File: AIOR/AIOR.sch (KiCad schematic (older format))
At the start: 92 parts, among them J1 Conn_01x06, J2 Conn_01x02, P1 CONN_02X20, P2 CONN_01X02, P3 CONN_01X04, P8 CONN_01X02, P9 CONN_01X04, U1 MCP2517FD, U2 ISO1050, U3 P82B715, U4 SI8641-SOIC, Y1 4MHz

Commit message: AIOR start
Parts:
- added D? (x2): BAT43, Diode_SMD:D_SOD-323_HandSoldering, symbol Diode:BAT43
- added R? (x3): 3k3, Resistors_SMD:R_0805_HandSolderingII, symbol AIOR-rescue:R
- added U?: DSPIC33EP128GM604, QFN/TQFP44, symbol dsPIC33EP128GM604:DSPIC33EP128GM604
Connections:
- net +3V3: now also U?.16 (BVDD)
- net GND: now also U?.9 (BGND)
- net GNDA: now also U?.16 (AVSS), U?.29 (VSS), U?.39 (VSS), U?.6 (VSS)
- net RxD: now also U?.13 (BOUT)
- net TxD: now also U?.12 (BDIN)
- net RS485_EN: now reaches U?.2 (~RE~), U?.3 (DE)
- net at U?.5 (AOUT): now also R?.2, U?.23 (PGEC1/OA1IN+/AN4/RPI34/RB2)
- net at U?.6 (ASCL): now also R?.2, U?.24 (PGED1/OA1IN-/AN5/CTMUC/RP35/RB3)
- new net: R?.1, U?.18 (~MCLR)
- new net: D?.1 (K), D?.2 (A), R?.2
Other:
- moved on the sheet: C6, C7, C8, C?, D?, J1, J2, J?, P8, P9, P?, Q?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

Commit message: wip
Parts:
- added C? (x4): 100nF, Capacitors_SMD:C_0805_HandSoldering, symbol AIOR-rescue:C
- added C? (x7): 1nF, Capacitors_SMD:C_0805_HandSoldering, symbol AIOR-rescue:C
- added C?: 560pF, Capacitors_SMD:C_0805_HandSoldering, symbol AIOR-rescue:C
- added D? (x2): 1N4148W, Diode_SMD:D_SOD-123, symbol Diode:1N4148W
- added Q? (x2): BC857, Package_TO_SOT_SMD:SOT-23, symbol Transistor_BJT:BC857
- added R?: 1M, Resistors_SMD:R_0805_HandSolderingII, symbol AIOR-rescue:R
- added R?: 2k2, Resistors_SMD:R_0805_HandSolderingII, symbol AIOR-rescue:R
- added R? (x3): 0, Resistors_SMD:R_0805_HandSolderingII, symbol AIOR-rescue:R
- added R? (x2): 3k3, Resistors_SMD:R_0805_HandSolderingII, symbol AIOR-rescue:R
- added R? (x2): 8k2, Resistors_SMD:R_0805_HandSolderingII, symbol AIOR-rescue:R
- added R?: 18k, Resistors_SMD:R_0805_HandSolderingII, symbol AIOR-rescue:R
- added R? (x2): 4k7, Resistors_SMD:R_0805_HandSolderingII, symbol AIOR-rescue:R
- added R?: 1k, Resistors_SMD:R_0805_HandSolderingII, symbol AIOR-rescue:R
- added U?: L7833, Package_TO_SOT_SMD:TO-252-3_TabPin2, symbol Regulator_Linear:L7805
- R?: value 10k -> 4k7
- renumbered C3 to C2, C1 to C3, R2 to R1, R1 to R2
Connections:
- net +5VA: now also C?.1, Q?.2 (E), R?.2
- net B_SENSE: now also R?.1, R?.2, U?.13 (P2.5/AD13), D?.1 (K), D?.2 (A), R?.1, R?.1, R?.1; no longer U?.6 (IS)
- net GNDA: now also U?.10 (TEST), U?.11 (VSSD), U?.6 (VSSA), U?.9 (MODE), C?.1, C?.2, C?.2, C?.2, C?.2, C?.2, C?.2, C?.2, C?.2, D?.1 (K), D?.2 (A), R?.1, R?.1, R?.1, U?.2 (GND)
- net VCC: now also C?.1, R?.2, U?.1 (IN)
- net Vccm: now reaches U?.11 (P2.7/AD15)
- net Vccm: now also C?.1, R?.1, R?.2
- net at U?.12 (P2.6/AD14): now also C?.1, R?.2
- net SUBC: now reaches U?.14 (P2.4/AD12)
- net SUBC: now also C?.1, Q?.3 (C), R?.2
- net RDDA: now reaches U?.19 (P1.7/AD7)
- net RDDA: now also U?.2 (RDDA)
- net RDCL: now reaches U?.20 (P1.6/AD6)
- net RDCL: now also U?.16 (RDCL)
- net QUAL: now reaches U?.21 (P1.5/AD5)
- net QUAL: now also U?.1 (QUAL)
- net at U?.29 (P0.5/UART0-RX): now also R?.1
- net at U?.30 (P0.4/UART0-TX): now also R?.1
- net IS_LEFT: now reaches R?.1, U?.6 (IS)
- net IS_LEFT: no longer R?.1, R?.2
- net at C?.1, U?.13 (OSCI), Y?.2: now also R?.2
- net at C?.1, Y?.1: now also R?.1, R?.1; no longer U?.14 (OSCO)
- net T57: now reaches U?.15 (T57)
- net at U?.3 (Vref): now also U?.4 (MUX), C?.1, C?.1
- net at U?.5 (VDDA): now also C?.1, R?.1
- net at U?.7 (CIN): now also C?.1
- net at U?.8 (SCOUT): now also C?.1, C?.2
- new net: R?.2, U?.14 (OSCO)
- new net: C?.2, R?.1
- new net: Q?.1 (B), Q?.2 (E), R?.2
- new net: Q?.1 (B), Q?.3 (C), R?.2
- new net: C?.2, C?.2, R?.2
- new net: C?.1, U?.3 (OUT)
- new net IS_RIGHT: R?.2, U?.6 (IS)
- no-connect marks 30 -> 32
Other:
- moved on the sheet: C?, R?, U?, Y?

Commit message: wip
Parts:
- removed D?: BAT43, Diode_SMD:D_SOD-323_HandSoldering, symbol Diode:BAT43
- removed J2: Conn_01x02, Pin_Headers:Pin_Header_Straight_1x02_Pitch2.54mm, symbol AIOR-rescue:Conn_01x02
- removed R8: 0, Resistors_SMD:R_0805_HandSolderingII, symbol AIOR-rescue:R
- removed R9: 50, Resistors_SMD:R_0805_HandSolderingII, symbol AIOR-rescue:R
- added C?: 10uF, Capacitor_SMD:C_Elec_5x5.8, symbol Device:CP
- added C? (x2): 100nF, Capacitors_SMD:C_0805_HandSoldering, symbol AIOR-rescue:C
- added D?: LED, LED_SMD:LED_0805_2012Metric_Pad1.15x1.40mm_HandSolder, symbol Device:LED
- added J?: 5V 12V, symbol Connector_Generic:Conn_01x03
- added P?: Selectrix, w_conn_jst-ph:s4b-ph-kl, symbol AIOR-rescue:CONN_01X04
- added Q?: BC817, Package_TO_SOT_SMD:SOT-23, symbol Transistor_BJT:BC817
- added R? (x2): 1k, Resistors_SMD:R_0805_HandSolderingII, symbol AIOR-rescue:R
- added R?: 470, Resistors_SMD:R_0805_HandSolderingII, symbol AIOR-rescue:R
- added R?: 0, Resistors_SMD:R_0805_HandSolderingII, symbol AIOR-rescue:R
- added R? (x2): 27k, Resistors_SMD:R_0805_HandSolderingII, symbol AIOR-rescue:R
- added R?: 120, Resistors_SMD:R_1206_HandSolderingII, symbol AIOR-rescue:R
- added R?: 1k5, Resistors_SMD:R_0805_HandSolderingII, symbol AIOR-rescue:R
- added U?: MCP2562, Package_SO:SOIC-8_3.9x4.9mm_P1.27mm, symbol AIOR-rescue:MCP2562
- added U?: 4504, Package_SO:SOIC-16_3.9x9.9mm_P1.27mm, symbol 4xxx:4504
- P?: value CONN_01X04 -> Xpressnet
- P?: value CONN_01X04 -> LOCONET
- R? (x2): value 470 -> 1k
- U?: value L7833 -> L7805
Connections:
- net +3V3: now also D?.2 (A), R?.1, R?.1, U?.1 (AVDD), U?.17 (AVDD), U?.28 (VDD), U?.40 (VDD), C?.1, C?.1, D?.2 (A), U?.5 (VIO~)
- net +5VA: now also U?.3 (VDD~)
- net B_ENA: now also U?.11 (RPI45/PWM2L/CTPLS/RB13)
- net B_LEFT: now also U?.14 (RPI46/PWM1H/T3CK/T7CK/RB14)
- net B_RIGHT: now also U?.15 (RPI47/PWM1L/T5CK/T6CK/RB15)
- net B_SENSE: now also U?.19 (OA2OUT/AN0/RPI16/RA0), R?.1; no longer R?.1, R?.2, R?.2
- net CANH: now also P3.4 (P4), R7.2, U2.7 (CANH), U?.7 (CANH); no longer P2.2 (P2), P3.3 (P3), U2.6 (CANL)
- net CANL: now also P2.2 (P2), P3.3 (P3), U2.6 (CANL), U?.6 (CANL); no longer P3.4 (P4), R7.2, U2.7 (CANH)
- net GND: no longer C6.2, C?.2, C?.2, Q?.2 (E), R?.1, R?.1, U4.2 (GND1), U4.8 (GND1), U?.4 (V-)
- net GNDA: now also C6.2, C?.2, C?.2, P?.1 (P1), Q?.2 (E), R?.1, R?.1, U4.2 (GND1), U4.8 (GND1), U?.4 (V-), U?.8 (AGND), C?.2, C?.2, C?.2, P?.1 (P1), Q?.2 (E), U?.2 (VSS~); no longer C7.2, C?.2, C?.2, J1.5 (Pin_5), U4.15 (GND2), U4.9 (GND2), U?.2 (GND)
- net GPIO17: now also U?.13 (BOUT)
- net GPIO4: now also U?.14 (BSDA)
- net LCNET: now also P?.3 (P3), P?.4 (P4)
- net LN_RX: now also U?.4 (RP56/PWM5H/RC8), R?.1; no longer R?.1, R?.2, R?.2, U?.1
- net LN_TX: now also U?.5 (RP57/PWM5L/RC9)
- net QUAL: now also U?.25 (OA3OUT/AN6/RP48/OCFB/RC0)
- net RDCL: now also U?.26 (OA3IN-/AN7/C3IN1-/C4IN1-/RP49/RC1)
- net RDDA: now also U?.27 (AN8/RPI50/U1RTS/BCLK1/FLT3/RC2)
- net RS485_EN: now also U?.10 (RPI44/PWM2H/RB12)
- net RS485_RX: now also U?.8 (RP42/PWM3H/RB10)
- net RS485_TX: now also U?.9 (RP43/PWM3L/RB11)
- net RxD: now also U?.11 (BSCL); no longer U?.13 (BOUT)
- net S88_CLK: now also U?.34 (OA5IN+/AN24/SDO1/RP20/T1CK/RA4)
- net S88_DATA: now also U?.32 (SDA2/RPI24/RA8)
- net S88_LOAD: now also U?.31 (OSC2/CLKO/RPI19/RA3)
- net S88_RST: now also U?.30 (AN32/OSC1/CLKI/RPI18/RA2)
- net VCC: now also C7.1, C?.1, U4.16 (VDD2), U?.3 (OUT), J?.1 (Pin_1), U?.1 (VCC), U?.13 (Select); no longer C?.1, U?.1 (IN)
- net VDDA: now also C?.1, U?.1 (IN), J?.3 (Pin_3); no longer C7.1, U4.16 (VDD2)
- net Vccm: now also U?.20 (OA2IN+/AN1/C2IN1+/RPI17/RA1)
- net at U4.11: now also R?.2
- net at U4.12: now also U?.7 (Cin)
- net at U4.13: now also U?.5 (Bin); no longer J1.3 (Pin_3)
- net at U4.14: now also U?.3 (Ain); no longer J1.2 (Pin_2)
- net at J1.6 (Pin_6): now also R?.1
- net at J1.4 (Pin_4): now also U?.6 (Cout)
- net PLED: now reaches U?.1 (TMS/OA5IN-/AN27/C5IN1-/RP41/RB9)
- net PLED: now also R?.2
- net at U?.2 (RP54/PWM6H/RC6): now also U?.1 (TXD)
- net XINT: now reaches U?.22 (PGEC3/AN3/RPI33/CTED1/RB1)
- net XINT: now also U?.4 (ADIN)
- net PGC: now reaches R?.2, U?.23 (PGEC1/OA1IN+/AN4/RPI34/RB2), U?.5 (AOUT)
- net PGC: now also R?.2
- net PGD: now reaches R?.2, U?.24 (PGED1/OA1IN-/AN5/CTMUC/RP35/RB3), U?.6 (ASCL)
- net PGD: now also R?.2
- net at U?.3 (RP55/PWM6L/RC7): now also U?.4 (RXD)
- net SLX_CK: now reaches U?.36 (AN29/SCK1/RPI51/RC3)
- net SLX_CK: now also R?.2
- net SLX_DI: now reaches U?.37 (AN30/SDA1/RPI52/RC4)
- net SLX_DI: now also R?.2
- net SLX_DO: now reaches U?.38 (AN31/CVREF2O/SCL1/RPI53/RC5)
- net SLX_DO: now also R?.2
- net at U?.7 (VCAP): now also C?.1
- net MCLR: now reaches D?.1 (K), R?.2
- net MCLR: now also U?.3 (ASDA)
- new net: U4.15 (GND2), U4.9 (GND2)
- new net: J1.2 (Pin_2), U?.2 (Aout)
- new net: J1.3 (Pin_3), U?.4 (Bout)
- new net: R?.1, R?.2, R?.2, R?.2, U?.1
- new net: R?.1, R?.2, R?.2, R?.2
- new net: D?.1 (K), R?.1
- new net: P?.2 (P2), R?.2
- new net: P?.3 (P3), R?.1
- new net: P?.4 (P4), R?.1
- new net: Q?.1 (B), R?.1
- new net: Q?.3 (C), R?.1
- new net: J?.2 (Pin_2), U?.16 (VDD)
- new net GNDS: C7.2, C?.2, C?.2, J1.5 (Pin_5), U?.2 (GND), U?.8 (VSS)
- no-connect marks 32 -> 49
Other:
- note removed: "GPIO Option"
- moved on the sheet: C2, C6, C7, C8, C?, D?, J1, J?, P8, P9, P?, Q?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

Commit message: add current sense transformer
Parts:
- added C85, C86: 100nF, Capacitors_SMD:C_0805_HandSoldering, symbol AIOR-rescue:C
- added J?: Conn_01x01, symbol Connector_Generic:Conn_01x01
- added R?: 0, Resistors_SMD:R_0805_HandSolderingII, symbol AIOR-rescue:R
- added TR?: 530x0c, Divers:530x0C, symbol 530x0c:530x0c
- gave numbers to parts that had none: 6
- renumbered C6 to C83, C7 to C84, J1 to J81, U4 to U82
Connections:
- net labels added: SLX_CL
- net labels removed: SLX_CK
- wire segments 606 -> 618
- no-connect marks 49 -> 48
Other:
- moved on the sheet: C81, C82, C83, C84, C?, J81, J82, J?, R81, R?, U81, U82A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

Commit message: wip
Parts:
- added C20, C21: 100nF, Capacitors_SMD:C_0805_HandSoldering, symbol AIOR-rescue:C
- added J1: Conn_01x02, Connector_PinHeader_2.54mm:PinHeader_1x02_P2.54mm_Vertical, symbol AIOR-rescue:Conn_01x02
- added J20: Conn_01x04, symbol Connector_Generic:Conn_01x04
- added J90: Conn_01x03, Connector_PinHeader_2.54mm:PinHeader_1x03_P2.54mm_Vertical, symbol Connector_Generic:Conn_01x03
- added U20: L7833, Package_TO_SOT_SMD:TO-252-3_TabPin2, symbol Regulator_Linear:L7805
- J50: renamed from J?; footprint (none) -> Connector_PinHeader_2.54mm:PinHeader_1x02_P2.54mm_Vertical
- TR30: renamed from TR?; symbol 530x0c:530x0c -> AIOR-rescue:530x0c-530x0c
- gave numbers to parts that had none: 108
- renumbered C2 to C1, C8 to C10, R7 to R3, U3 to U4
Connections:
- net labels added: HBL, HBR, RB5, RB6, RB7, RB8
- wire segments 618 -> 636
- no-connect marks 48 -> 53
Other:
- note added: "S88"
- moved on the sheet: C23, C24, C27, C30, C31, J30, R22, R23, R24, R25, R30, R31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

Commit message: wip
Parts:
- removed U22: DSPIC33EP128GM604, QFN/TQFP44, symbol dsPIC33EP128GM604:DSPIC33EP128GM604
- added C27, C28: 22pF, Capacitors_SMD:C_0805_HandSoldering, symbol AIOR-rescue:C
- added U22: DSPIC33EP128GM604-dsPIC33EP128GM604_copy, QFN/TQFP44, symbol AIOR-rescue:DSPIC33EP128GM604-dsPIC33EP128GM604_copy-dsPIC33EP128GM604-AIOR-res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
- added Y20: 8MHz, w_crystal:crystal_hc-49s, symbol AIOR-rescue:Crystal
- J20: footprint (none) -> Connector_PinHeader_2.54mm:PinHeader_1x04_P2.54mm_Vertical
- J70: footprint (none) -> Connector_PinHeader_2.54mm:PinHeader_1x01_P2.54mm_Vertical
- U24, U42, U50: footprint Package_SO:SOIC-8_3.9x4.9mm_P1.27mm -> w_smd_dil:so-8
- U41, U70: footprint (none) -> w_smd_dil:so-8
- U90: symbol adum1251:SAA6579 -> AIOR-rescue:SAA6579-adum1251
- renumbered C27 to C29
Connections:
- net +3V3: now also U22.17 (AVDD), U22.28 (VDD), U22.40 (VDD)
- net B_ENA: now also U22.11 (RPI45/PWM2L/CTPLS/RB13)
- net B_LEFT: now also U22.14 (RPI46/PWM1H/T3CK/T7CK/RB14)
- net B_RIGHT: now also U22.15 (RPI47/PWM1L/T5CK/T6CK/RB15)
- net B_SENSE: now also U22.19 (OA2OUT/AN0/RPI16/RA0)
- net GND: now also C27.2, C28.2
- net GNDA: now also U22.16 (AVSS), U22.29 (VSS), U22.39 (VSS), U22.6 (VSS)
- net LN_RX: now also U22.4 (RP56/PWM5H/RC8)
- net LN_TX: now also U22.5 (RP57/PWM5L/RC9)
- net PGC: now also U22.23 (PGEC1/OA1IN+/AN4/RPI34/RB2)
- net PGD: now also U22.24 (PGED1/OA1IN-/AN5/CTMUC/RP35/RB3)
- net PLED: now also U22.1 (TMS/OA5IN-/AN27/C5IN1-/RP41/RB9)
- net QUAL: now also U22.25 (OA3OUT/AN6/RP48/OCFB/RC0)
- net RB5: now also U22.41 (PGED2/ASDA2/RP37/RB5)
- net RB6: now also U22.42 (PGEC2/ASCL2/RP38/RB6)
- net RB7: now also U22.43 (OA5OUT/AN25/C5IN4-/RP39/INT0/RB7)
- net RB8: now also U22.44 (CVREF1O/ASCL1/RP40/T4CK/RB8)
- net RDCL: now also U22.26 (OA3IN-/AN7/C3IN1-/C4IN1-/RP49/RC1)
- net RDDA: now also U22.27 (AN8/RPI50/U1RTS/BCLK1/FLT3/RC2)
- net RS485_EN: now also U22.10 (RPI44/PWM2H/RB12)
- net RS485_RX: now also U22.8 (RP42/PWM3H/RB10)
- net RS485_TX: now also U22.9 (RP43/PWM3L/RB11)
- net S88_CLK: now also U22.34 (OA5IN+/AN24/SDO1/RP20/T1CK/RA4)
- net S88_DATA: now also U22.35 (AN28/ASDA1/SDI1/RPI25/RA9)
- net S88_LOAD: now also U22.33 (FLT32/SCL2/RP36/RB4)
- net S88_RST: now also U22.32 (SDA2/RPI24/RA8)
- net SLX_CL: now also U22.36 (AN29/SCK1/RPI51/RC3)
- net SLX_DI: now also U22.37 (AN30/SDA1/RPI52/RC4)
- net SLX_DO: now also U22.38 (AN31/CVREF2O/SCL1/RPI53/RC5)
- net Vccm: now also U22.20 (OA2IN+/AN1/C2IN1+/RPI17/RA1)
- net XINT: now also U22.22 (PGEC3/AN3/RPI33/CTED1/RB1)
- net at R20.1: now also U22.18 (~MCLR)
- net at U24.1 (TXD): now also U22.2 (RP54/PWM6H/RC6)
- net at U24.4 (RXD): now also U22.3 (RP55/PWM6L/RC7)
- net at C22.1: now also U22.7 (VCAP)
- net at C96.1, U90.3 (Vref): now also C95.1, U90.4 (MUX)
- new net: C27.1, U22.30 (AN32/OSC1/CLKI/RPI18/RA2), Y20.2
- new net: C28.1, U22.31 (OSC2/CLKO/RPI19/RA3), Y20.1
- no-connect marks 53 -> 51
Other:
- moved on the sheet: C90, C91, C92, C93, C94, C95, C96, C97, C98, C99, D21, D90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

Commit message: wip
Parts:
- removed J30: Conn_01x02, symbol AIOR-rescue:Conn_01x02
- added J30, J31: Conn_01x01, Connector:Banana_Jack_1Pin, symbol Connector_Generic:Conn_01x01
- C1, C10, C2, C20, C21, C23, C24, C25, C26, C27, C28, C29, C3, C30, C31, C4, C40, C41, C42, C43, C44, C45, C46, C5, C70, C71, C72, C81, C82, C83, C84, C85, C86, C90, C91, C92, C93, C94, C95, C96, C97, C98, C99: footprint Capacitors_SMD:C_0805_HandSoldering -> Capacitor_SMD:C_0805_2012Metric_Pad1.15x1.40mm_HandSolder
- J81: footprint Pin_Headers:Pin_Header_Angled_1x06_Pitch2.54mm -> Connector_PinHeader_2.54mm:PinHeader_1x06_P2.54mm_Horizontal
- J82: footprint (none) -> Connector_PinHeader_2.54mm:PinHeader_1x03_P2.54mm_Vertical
- P2, P8: footprint Pin_Headers:Pin_Header_Angled_1x02 -> Connector_PinHeader_2.54mm:PinHeader_1x02_P2.54mm_Vertical
- Q60, Q70, Q90, Q91: footprint Package_TO_SOT_SMD:SOT-23 -> Package_TO_SOT_SMD:SOT-23_Handsoldering
- R1, R10, R11, R12, R13, R2, R20, R21, R22, R23, R24, R25, R30, R31, R32, R33, R34, R35, R36, R37, R40, R400, R401, R41, R42, R43, R44, R45, R46, R47, R48, R49, R50, R51, R60, R61, R63, R702, R703, R71, R72, R74, R75, R76, R77, R78, R79, R81, R90, R91, R92, R93, R94, R95, R96: footprint Resistors_SMD:R_0805_HandSolderingII -> Resistor_SMD:R_0805_2012Metric_Pad1.15x1.40mm_HandSolder
- R3, R62: footprint Resistors_SMD:R_1206_HandSolderingII -> Resistor_SMD:R_0805_2012Metric_Pad1.15x1.40mm_HandSolder
- R52, R700, R701: footprint Resistors_SMD:R_1206_HandSolderingII -> Resistor_SMD:R_1206_3216Metric_Pad1.42x1.75mm_HandSolder
- TR30: footprint Divers:530x0C -> Diverse:530x0C
- U22: value DSPIC33EP128GM604-dsPIC33EP128GM604_copy -> DSPIC33EP128GM604; footprint QFN/TQFP44 -> Package_QFP:LQFP-44_10x10mm_P0.8mm
- U83: footprint Package_SO:SOIC-16_3.9x9.9mm_P1.27mm -> w_smd_dil:so-16
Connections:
- net HBL: now also J30.1 (Pin_1)
- net HBR: now also J31.1 (Pin_1)

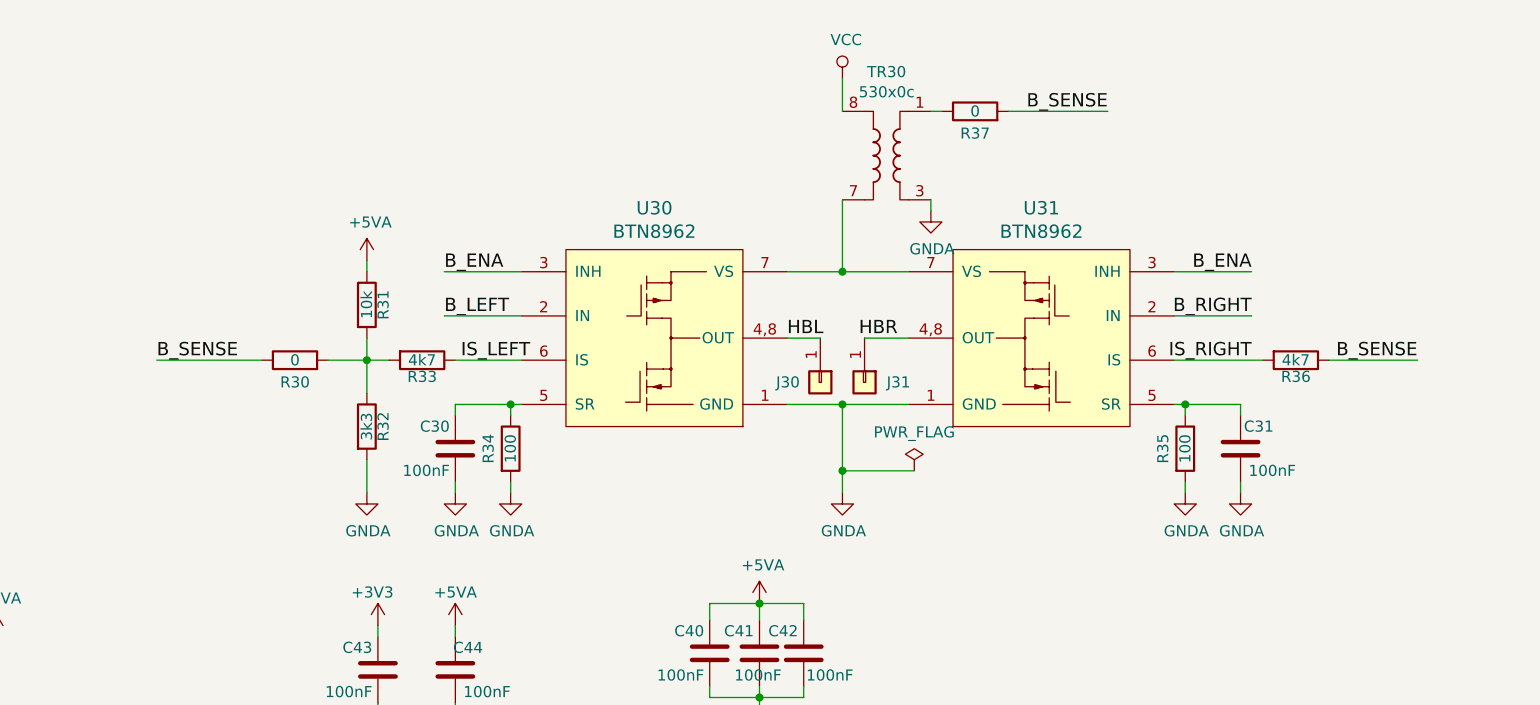
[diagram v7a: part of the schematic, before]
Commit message: use existing BTN89082 lib
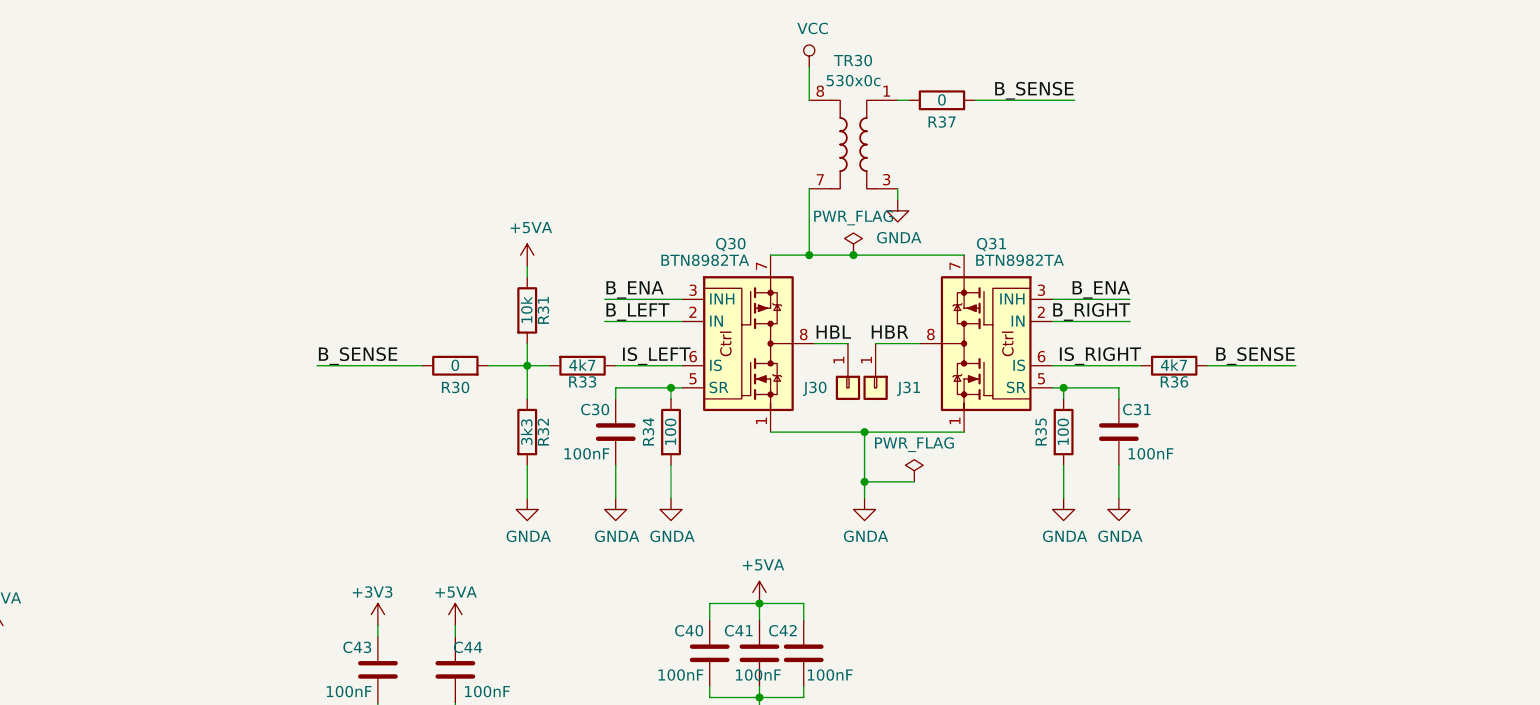
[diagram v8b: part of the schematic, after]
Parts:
- removed U30, U31: BTN8962, Package_TO_SOT_SMD:TO-263-7_TabPin8, symbol BTN8962:BTN8962
- added Q30, Q31: BTN8982TA, Package_TO_SOT_SMD:TO-263-7_TabPin8, symbol Power_Management:BTN8982TA
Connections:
- net B_ENA: now also Q30.3 (INH), Q31.3 (INH)
- net B_LEFT: now also Q30.2 (IN)
- net B_RIGHT: now also Q31.2 (IN)
- net GNDA: now also Q30.1, Q31.1
- net HBL: now also Q30.4, Q30.8
- net HBR: now also Q31.4, Q31.8
- net IS_LEFT: now also Q30.6 (IS)
- net IS_RIGHT: now also Q31.6 (IS)
- net at C30.1, R34.1: now also Q30.5 (SR)
- net at C31.1, R35.1: now also Q31.5 (SR)
- net at TR30.7: now also Q30.7, Q31.7
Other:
- moved on the sheet: C30, C31, J30, J31, R30, R31, R32, R33, R34, R35, R36, R37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
